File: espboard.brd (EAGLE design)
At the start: 61.8 x 64.9 mm, 39 parts

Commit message: split board into three parts, cam processed
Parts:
- removed AMP: AZV321, Diodes_Inc_By_element14_Batch_1:SOT65P210X110-5N
- removed C1: 2.2uF, Seeed-OPL-Capacitor:C0603
- removed C2: 22uF, Seeed-OPL-Capacitor:C0603
- removed CONN: BOURNS_2PIN, CUSTOM:BOURNS_2PIN
- removed D1: B130-13-F, CUSTOM:SMA
- removed L1: DFE252012C, CUSTOM:1008
- removed MICRO-USB: ZX80-B-5P, CUSTOM:USB_VERT
- removed R10: 100k, resistor:R0603
- removed R8: 1k, resistor:R0603
- removed R9: 5k, resistor:R0603
- removed REG: TPS62177, CUSTOM:WSON-10
- removed U$3: 4PIN_HEADER, CUSTOM:4PIN_HEADER
- removed WIPER: BOURNS_4PIN, CUSTOM:BOURNS_4PIN
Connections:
- removed net N$2: R10.1, REG.7
- removed net N$5: AMP.1, WIPER.P4
- removed net N$6: AMP.3, R8.2, R9.1
- removed net SW: L1.P$2, REG.9
- removed net USB+: D1.AN, MICRO-USB.VCC, U$3.1
- net +3V3: no longer AMP.5, C2.2, L1.P$3, R10.2, REG.10, REG.8
- net ADC: no longer AMP.4, R9.2
- net D+: no longer MICRO-USB.D+, U$3.3
- net D-: no longer MICRO-USB.D-, U$3.2
- net GND: no longer AMP.2, C1.1, C2.1, CONN.P2, MICRO-USB.GND, MICRO-USB.GND1, MICRO-USB.GND2, MICRO-USB.GND3, MICRO-USB.GND4, R8.1, REG.1, REG.11, REG.4, REG.5, REG.6, U$3.4, WIPER.P1, WIPER.P2
- net VCC: no longer C1.2, CONN.P1, D1.CATH, REG.2, REG.3, WIPER.P3
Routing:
- net VCC: track 82.4 -> 24.4 mm, vias 3 -> 1
- net N$5: track 25.0 -> 0.00 mm, vias 2 -> 0
- net +3V3: track 134.0 -> 110.4 mm, vias 7 -> 6
- net ADC: track 18.0 -> 12.5 mm, vias 2 -> 1
- net N$6: track 5.15 -> 0.00 mm
- net SW: track 2.57 -> 0.00 mm
- net N$2: track 2.04 -> 0.00 mm
- net D-: vias 3 -> 2
- net D+: vias 3 -> 2
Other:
- board size 61.8 x 64.9 mm -> 61.8 x 22.5 mm

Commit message: final cad for purchase
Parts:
- moved R4 0.50 mm to (25.0, 6.50)
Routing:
- net GP2: track 3.65 -> 3.15 mm
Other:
- board text added: "ESP-12"
- board text added: "GND"
- board text added: "M"
- board text added: "SIG"
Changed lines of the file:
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@@
 <text x="59" y="19" size="1.016" layer="21">VCC</text>
 <text x="47" y="19" size="1.016" layer="21">3V3</text>
+<text x="51" y="19" size="0.8128" layer="21">GND</text>
+<text x="43" y="21" size="0.8128" layer="21">SIG</text>
+<text x="56.2" y="19.7" size="0.8128" layer="21">M</text>
+<text x="34" y="2" size="1.27" layer="21">ESP-12</text>
 </plain>
 <attributes>
@@
 </element>
 <element name="DRIVER" library="CUSTOM" package="SSOP-20" value="TB6593FNG" x="52" y="15" smashed="yes" rot="R180">
-<attribute name="NAME" x="55.2994" y="19.93" size="1.016" layer="25" ratio="10" rot="SR180"/>
+<attribute name="NAME" x="54.2994" y="10.93" size="1.016" layer="25" ratio="10" rot="SR180"/>
 <attribute name="VALUE" x="55.4544" y="22.62" size="2.0828" layer="27" ratio="10" rot="SR180"/>
 </element>
@@
 <attribute name="VALUE" x="27.69" y="3.925" size="1.27" layer="27" rot="R180"/>
 </element>
-<element name="R4" library="resistor" package="R0603" value="10k" x="25" y="7" smashed="yes" rot="MR180">
-<attribute name="NAME" x="23.695" y="6.165" size="1.27" layer="26" rot="MR180"/>
-<attribute name="VALUE" x="24.365" y="8.905" size="1.27" layer="28" rot="MR180"/>
+<element name="R4" library="resistor" package="R0603" value="10k" x="25" y="6.5" smashed="yes" rot="MR180">
+<attribute name="NAME" x="23.695" y="5.665" size="1.27" layer="26" rot="MR180"/>
+<attribute name="VALUE" x="24.365" y="8.405" size="1.27" layer="28" rot="MR180"/>
 </element>
 <element name="C7" library="Seeed-OPL-Capacitor" package="C0603" value="10uF" x="46.5" y="15" smashed="yes">
@@
 <attribute name="NAME" x="34.746" y="14.73" size="0.635" layer="34" ratio="10" rot="MR90"/>
 </element>
-<element name="U$2" library="CUSTOM" package="BI_LED" value="BI_LED" x="26.998" y="12.03" rot="MR90"/>
+<element name="U$2" library="CUSTOM" package="BI_LED" value="BI_LED" x="27" y="12" rot="MR90"/>
 <element name="R11" library="resistor" package="R0603" value="100" x="31" y="15" smashed="yes" rot="MR90">
 <attribute name="NAME" x="30.435" y="10.265" size="1.27" layer="26" rot="MR90"/>
@@
 <via x="7.4" y="13.9" extent="1-16" drill="0.6"/>
 <via x="54" y="10" extent="1-16" drill="0.6"/>
-<via x="31" y="10" extent="1-16" drill="0.6"/>
+<via x="26" y="14" extent="1-16" drill="0.6"/>
 <via x="35" y="11" extent="1-16" drill="0.6"/>
 </signal>
@@
 <wire x1="33" y1="14" x2="33" y2="7" width="1.016" layer="16"/>
 <wire x1="33" y1="7" x2="31.85" y2="7" width="1.016" layer="16"/>
-<wire x1="24.15" y1="7" x2="24" y2="7" width="1.016" layer="16"/>
+<wire x1="24.15" y1="6.5" x2="24" y2="6.5" width="1.016" layer="16"/>
 <wire x1="48.3678" y1="12.079" x2="47.079" y2="12.079" width="0.4064" layer="1"/>
 <wire x1="47.079" y1="12.079" x2="46" y2="11" width="0.4064" layer="1"/>
@@
 <wire x1="46" y1="11" x2="46.738" y2="11" width="0.8128" layer="1"/>
 <wire x1="46.738" y1="11" x2="46.738" y2="10" width="0.8128" layer="1"/>
-<wire x1="24" y1="7" x2="18" y2="7" width="0.8128" layer="16"/>
-<via x="18" y="7" extent="1-16" drill="0.6"/>
-<wire x1="18" y1="7" x2="15.9" y2="7" width="0.8128" layer="1"/>
+<wire x1="24" y1="6.5" x2="18" y2="6.5" width="0.8128" layer="16"/>
+<via x="18" y="6.5" extent="1-16" drill="0.6"/>
 <wire x1="15.9" y1="7" x2="15.9" y2="7.46" width="0.8128" layer="1"/>
-<wire x1="18" y1="7" x2="18.238" y2="7" width="0.8128" layer="1"/>
-<wire x1="18.238" y1="7" x2="18.238" y2="5" width="0.8128" layer="1"/>
+<wire x1="18" y1="6.5" x2="18.238" y2="6.5" width="0.8128" layer="1"/>
+<wire x1="18.238" y1="6.5" x2="18.238" y2="5" width="0.8128" layer="1"/>
 <wire x1="12.365" y1="15.46" x2="12.5" y2="15.46" width="0.6096" layer="1"/>
 <wire x1="12.5" y1="15.46" x2="12.5" y2="17" width="0.6096" layer="1"/>
@@
 <wire x1="33" y1="5" x2="24.2" y2="5" width="0.8128" layer="16"/>
 <wire x1="24.2" y1="5" x2="24.15" y2="5.15" width="0.8128" layer="16"/>
-<wire x1="24.15" y1="5.15" x2="24.15" y2="7" width="0.8128" layer="16"/>
+<wire x1="24.15" y1="5.15" x2="24.15" y2="6.5" width="0.8128" layer="16"/>
 <wire x1="40.85" y1="18" x2="41" y2="17.85" width="0.8128" layer="16"/>
 <wire x1="41" y1="17.85" x2="41" y2="17" width="0.8128" layer="16"/>
 <via x="41" y="17" extent="1-16" drill="0.6"/>
 <wire x1="41" y1="17" x2="41" y2="16" width="0.8128" layer="1"/>
+<wire x1="18" y1="6.5" x2="15.9" y2="6.5" width="0.8128" layer="1"/>
+<wire x1="15.9" y1="6.5" x2="15.9" y2="7.46" width="0.8128" layer="1"/>
 <wire x1="8.555" y1="17" x2="9.238" y2="17" width="0" layer="19" extent="1-16"/>
 </signal>
@@
 <wire x1="13.635" y1="14.2" x2="13.6" y2="14.2" width="0.6096" layer="1"/>
 <via x="13.6" y="14.2" extent="1-16" drill="0.6"/>
-<wire x1="13.6" y1="14.2" x2="13.6" y2="15" width="0.6096" layer="16"/>
-<wire x1="13.6" y1="15" x2="7" y2="15" width="0.6096" layer="16"/>
-<wire x1="7" y1="15" x2="6" y2="16" width="0.6096" layer="16"/>
-<wire x1="6" y1="16" x2="6" y2="18" width="0.6096" layer="16"/>
+<wire x1="13.6" y1="14.2" x2="13.6" y2="15" width="0.4064" layer="16"/>
+<wire x1="13.6" y1="15" x2="7" y2="15" width="0.4064" layer="16"/>
+<wire x1="7" y1="15" x2="6" y2="16" width="0.4064" layer="16"/>
+<wire x1="6" y1="16" x2="6" y2="18" width="0.4064" layer="16"/>
 </signal>
 <signal name="D-">
@@
 <via x="14.9" y="14.2" extent="1-16" drill="0.6"/>
 <wire x1="14.9" y1="14.2" x2="15" y2="14.3" width="0.6096" layer="16"/>
-<wire x1="15" y1="14.3" x2="15" y2="16" width="0.6096" layer="16"/>
-<wire x1="15" y1="16" x2="8" y2="16" width="0.6096" layer="16"/>
-<wire x1="8" y1="16" x2="7.5" y2="16.5" width="0.6096" layer="16"/>
-<wire x1="7.5" y1="16.5" x2="7.5" y2="21" width="0.6096" layer="16"/>
-<wire x1="7.5" y1="21" x2="6" y2="21" width="0.6096" layer="16"/>
+<wire x1="15" y1="14.3" x2="15" y2="16" width="0.4064" layer="16"/>
+<wire x1="15" y1="16" x2="8" y2="16" width="0.4064" layer="16"/>
+<wire x1="8" y1="16" x2="7.5" y2="16.5" width="0.4064" layer="16"/>
+<wire x1="7.5" y1="16.5" x2="7.5" y2="21" width="0.4064" layer="16"/>
+<wire x1="7.5" y1="21" x2="6" y2="21" width="0.4064" layer="16"/>
 </signal>
 <signal name="STBY">
@@
 <contactref element="R4" pad="2"/>
 <contactref element="ESP12" pad="11"/>
-<wire x1="27" y1="4.5" x2="27" y2="7" width="1.016" layer="1"/>
-<via x="27" y="7" extent="1-16" drill="0.6"/>
-<wire x1="27" y1="7" x2="25.85" y2="7" width="1.016" layer="16"/>
+<wire x1="27" y1="4.5" x2="27" y2="6.5" width="1.016" layer="1"/>
+<via x="27" y="6.5" extent="1-16" drill="0.6"/>
+<wire x1="27" y1="6.5" x2="25.85" y2="6.5" width="1.016" layer="16"/>
 </signal>
 <signal name="N$8">
@@
 <contactref element="R11" pad="1"/>
 <contactref element="U$2" pad="2"/>
-<wire x1="28.948" y1="11.53" x2="31" y2="11.53" width="0.4064" layer="16"/>
-<wire x1="31" y1="11.53" x2="31" y2="14.15" width="0.4064" layer="16"/>
+<wire x1="28.95" y1="11.5" x2="31" y2="11.5" width="0.4064" layer="16"/>
+<wire x1="31" y1="11.5" x2="31" y2="14.15" width="0.4064" layer="16"/>
 </signal>
 <signal name="N$12">
 <contactref element="R12" pad="1"/>
 <contactref element="U$2" pad="3"/>
-<wire x1="28.948" y1="12.53" x2="29" y2="12.53" width="0.4064" layer="16"/>
+<wire x1="28.95" y1="12.5" x2="29" y2="12.53" width="0.4064" layer="16"/>
 <wire x1="29" y1="12.53" x2="29" y2="14.15" width="0.4064" layer="16"/>
 </signal>

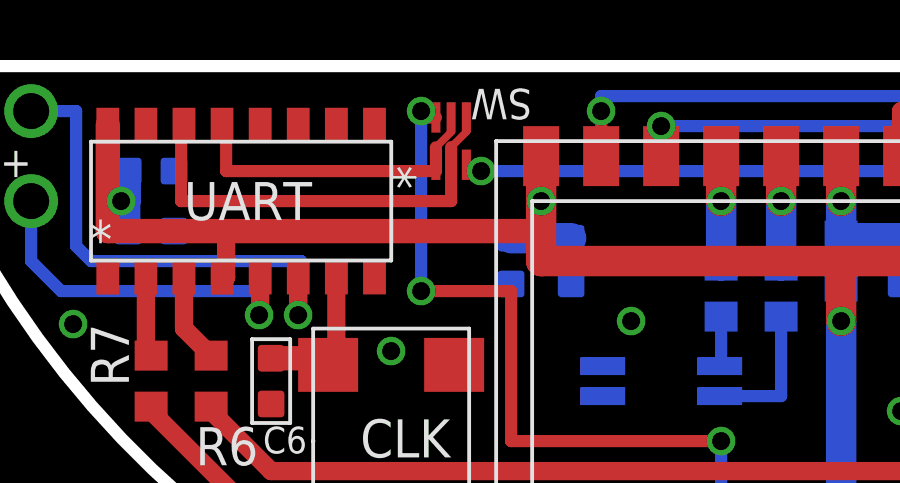
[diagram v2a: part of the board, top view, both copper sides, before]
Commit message: fixed intial board errors, including short, flipped usb, and missing trace
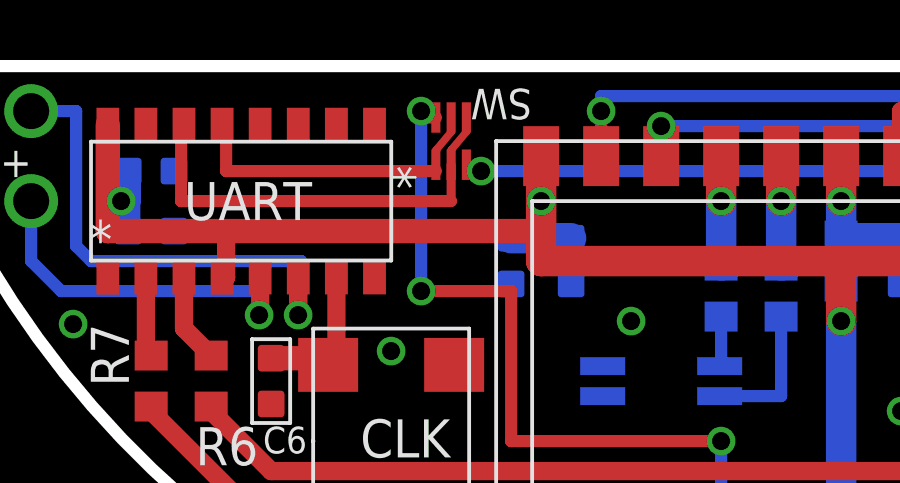
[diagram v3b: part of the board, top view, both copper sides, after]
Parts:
- R11, R12: value 100 -> 330
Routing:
- net RTS: track 15.2 -> 14.6 mm
- net DTR: track 11.2 -> 10.6 mm
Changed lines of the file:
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@@
 <layer number="20" name="Dimension" color="15" fill="1" visible="yes" active="yes"/>
 <layer number="21" name="tPlace" color="7" fill="1" visible="yes" active="yes"/>
-<layer number="22" name="bPlace" color="7" fill="1" visible="yes" active="yes"/>
-<layer number="23" name="tOrigins" color="15" fill="1" visible="yes" active="yes"/>
-<layer number="24" name="bOrigins" color="15" fill="1" visible="yes" active="yes"/>
+<layer number="22" name="bPlace" color="7" fill="1" visible="no" active="yes"/>
+<layer number="23" name="tOrigins" color="15" fill="1" visible="no" active="yes"/>
+<layer number="24" name="bOrigins" color="15" fill="1" visible="no" active="yes"/>
 <layer number="25" name="tNames" color="7" fill="1" visible="yes" active="yes"/>
 <layer number="26" name="bNames" color="7" fill="1" visible="yes" active="yes"/>
 <layer number="27" name="tValues" color="7" fill="1" visible="no" active="yes"/>
 <layer number="28" name="bValues" color="7" fill="1" visible="no" active="yes"/>
-<layer number="29" name="tStop" color="7" fill="3" visible="yes" active="yes"/>
-<layer number="30" name="bStop" color="7" fill="6" visible="yes" active="yes"/>
+<layer number="29" name="tStop" color="7" fill="3" visible="no" active="yes"/>
+<layer number="30" name="bStop" color="7" fill="6" visible="no" active="yes"/>
 <layer number="31" name="tCream" color="7" fill="4" visible="no" active="yes"/>
 <layer number="32" name="bCream" color="7" fill="5" visible="no" active="yes"/>
@@
 <layer number="155" name="FabDoc3" color="7" fill="15" visible="no" active="no"/>
 <layer number="199" name="Contour" color="7" fill="1" visible="no" active="yes"/>
-<layer number="200" name="200bmp" color="1" fill="10" visible="yes" active="yes"/>
+<layer number="200" name="200bmp" color="1" fill="10" visible="no" active="yes"/>
 <layer number="201" name="201bmp" color="2" fill="1" visible="no" active="no"/>
 <layer number="202" name="202bmp" color="3" fill="1" visible="no" active="no"/>
@@
 </element>
 <element name="U$2" library="CUSTOM" package="BI_LED" value="BI_LED" x="27" y="12" rot="MR90"/>
-<element name="R11" library="resistor" package="R0603" value="100" x="31" y="15" smashed="yes" rot="MR90">
+<element name="R11" library="resistor" package="R0603" value="330" x="31" y="15" smashed="yes" rot="MR90">
 <attribute name="NAME" x="30.435" y="10.265" size="1.27" layer="26" rot="MR90"/>
 <attribute name="VALUE" x="29.095" y="14.365" size="1.27" layer="28" rot="MR90"/>
 </element>
-<element name="R12" library="resistor" package="R0603" value="100" x="29" y="15" smashed="yes" rot="MR90">
+<element name="R12" library="resistor" package="R0603" value="330" x="29" y="15" smashed="yes" rot="MR90">
 <attribute name="NAME" x="26.835" y="14.165" size="1.27" layer="26" rot="MR90"/>
 <attribute name="VALUE" x="27.095" y="14.365" size="1.27" layer="28" rot="MR90"/>
@@
 <contactref element="UART" pad="14"/>
 <wire x1="20.508" y1="20.7874" x2="20.508" y2="20.308" width="0.254" layer="1"/>
-<wire x1="20.508" y1="20.308" x2="20" y2="19.8" width="0.254" layer="1"/>
-<wire x1="20" y1="19.8" x2="20" y2="19.2126" width="0.254" layer="1"/>
-<wire x1="20" y1="19.8" x2="20" y2="18" width="0.4064" layer="1"/>
+<wire x1="20.508" y1="20.308" x2="20" y2="19.7" width="0.254" layer="1"/>
+<wire x1="20" y1="19.7" x2="20" y2="19.2126" width="0.254" layer="1"/>
 <wire x1="20" y1="18" x2="11" y2="18" width="0.4064" layer="1"/>
 <wire x1="11" y1="18" x2="11" y2="20.54" width="0.4064" layer="1"/>
 <wire x1="11" y1="20.54" x2="11.095" y2="20.54" width="0.4064" layer="1"/>
+<wire x1="20" y1="18" x2="20" y2="19.2126" width="0.3048" layer="1"/>
 </signal>
 <signal name="DTR">
@@
 <contactref element="SW" pad="5"/>
 <contactref element="UART" pad="13"/>
-<wire x1="19.492" y1="19.2126" x2="19.492" y2="19.792" width="0.254" layer="1"/>
-<wire x1="19.492" y1="19.792" x2="20" y2="20.3" width="0.254" layer="1"/>
+<wire x1="19.492" y1="19.692" x2="20" y2="20.3" width="0.254" layer="1"/>
 <wire x1="20" y1="20.3" x2="20" y2="20.7874" width="0.254" layer="1"/>
-<wire x1="19.492" y1="19.792" x2="19.492" y2="19" width="0.4064" layer="1"/>
 <wire x1="19.492" y1="19" x2="12.5" y2="19" width="0.4064" layer="1"/>
 <wire x1="12.5" y1="19" x2="12.5" y2="20.54" width="0.4064" layer="1"/>
 <wire x1="12.5" y1="20.54" x2="12.365" y2="20.54" width="0.4064" layer="1"/>
+<wire x1="19.492" y1="19" x2="19.492" y2="19.692" width="0.254" layer="1"/>
+<wire x1="19.492" y1="19" x2="19.492" y2="19.2126" width="0" layer="19" extent="1-1"/>
 </signal>
 <signal name="XI">
